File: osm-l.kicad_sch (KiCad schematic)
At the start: 48 parts, among them SW1 SW_KMR211NGLFS_SMD, SW2 SW_KMR211NGLFS_SMD, SW3 SW_KMR211NGLFS_SMD, U1 OSM-L_Carrier-side, U2 74AUP2G132, U3 74AUP2G132

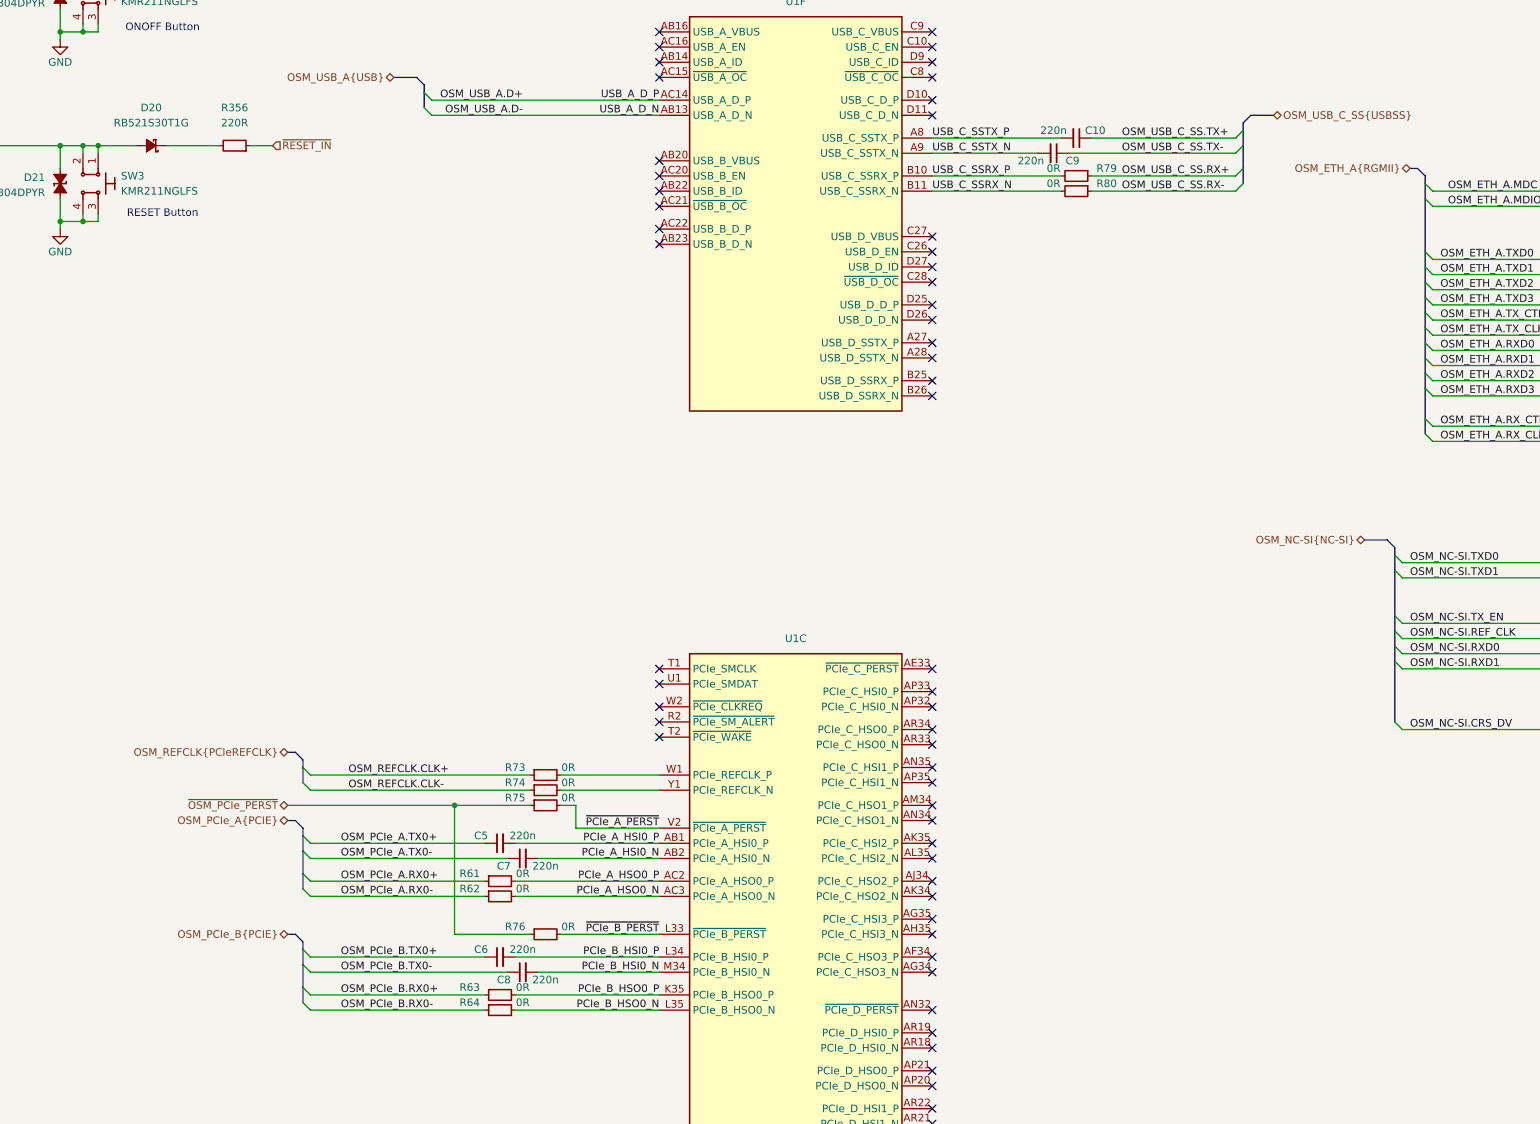
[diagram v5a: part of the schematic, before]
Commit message: [#83767] Remove PCIe/USB SS passives
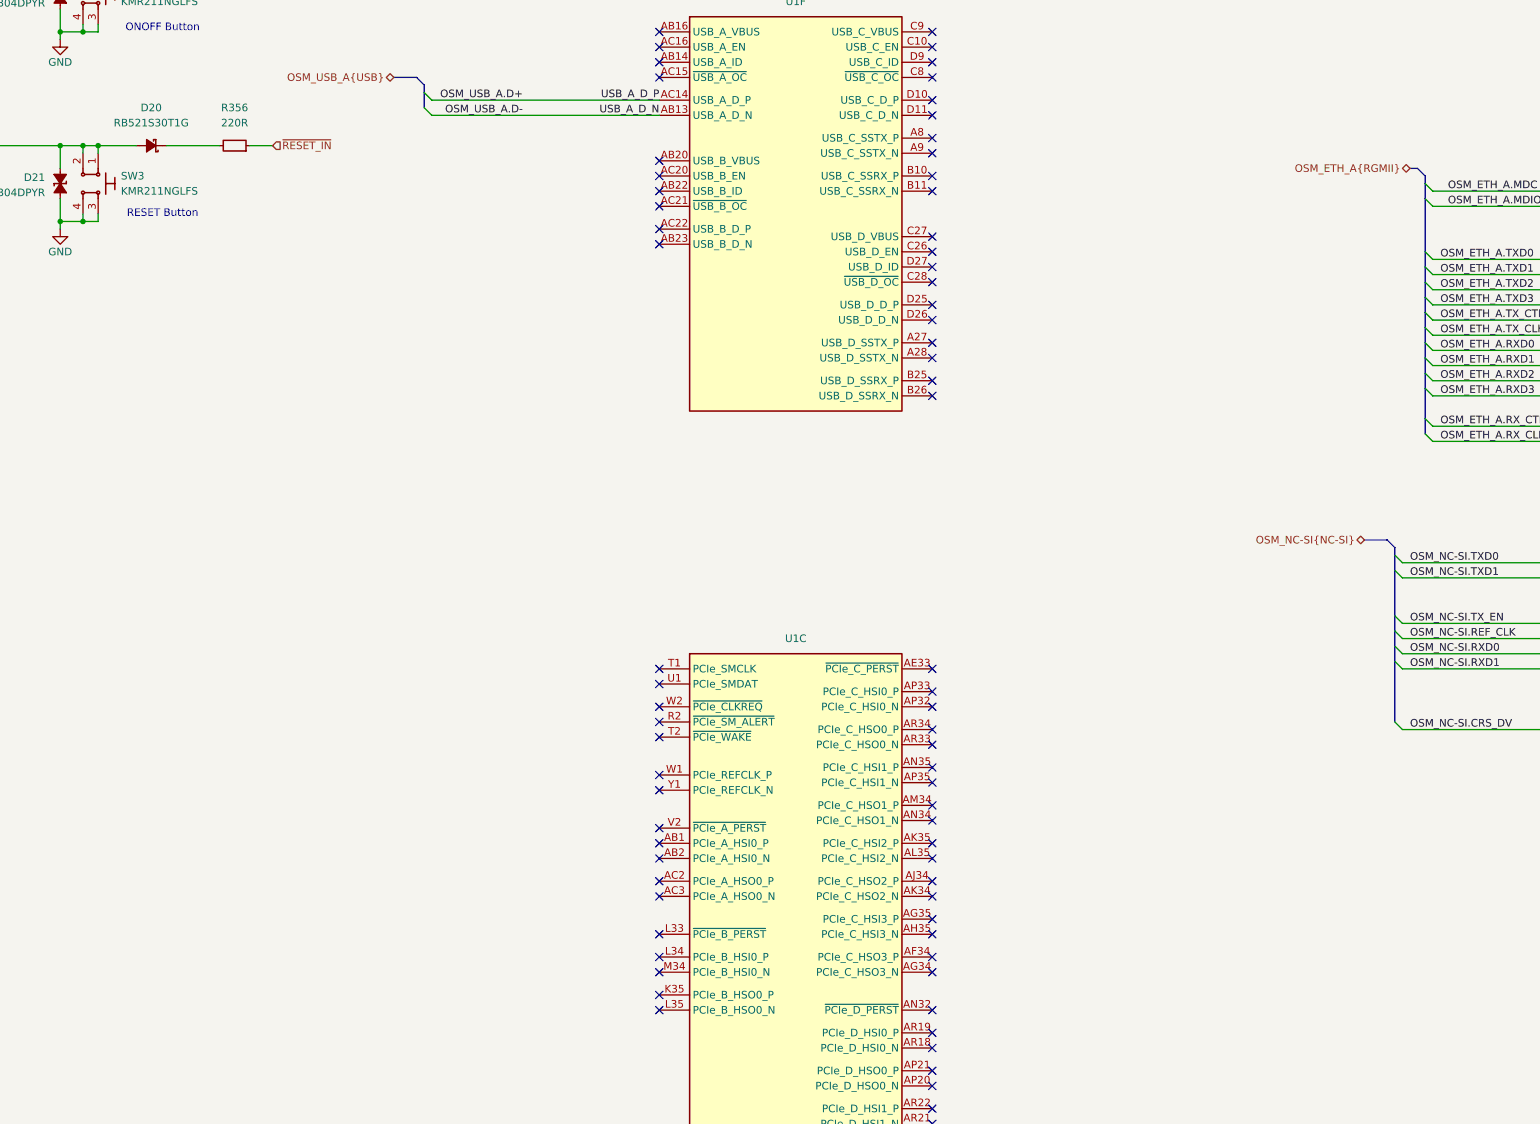
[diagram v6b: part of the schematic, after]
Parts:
- removed C10, C5, C6, C7, C8, C9: C_220n_0402, antmicro-footprints:C_0402_1005Metric, symbol antmicroCapacitors0402:C_220n_0402
- removed R61, R62, R63, R64, R73, R74, R75, R76, R79, R80: R_0R_0402, antmicro-footprints:R_0402_1005Metric, symbol antmicroResistors0402:R_0R_0402
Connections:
- net PCIe_A_HSI0_N: no longer names the net of U1.AB2 (PCIe_A_HSI0_N)
- net PCIe_A_HSI0_P: no longer names the net of U1.AB1 (PCIe_A_HSI0_P)
- net PCIe_A_HSO0_N: no longer names the net of U1.AC3 (PCIe_A_HSO0_N)
- net PCIe_A_HSO0_P: no longer names the net of U1.AC2 (PCIe_A_HSO0_P)
- net PCIe_B_HSI0_N: no longer names the net of U1.M34 (PCIe_B_HSI0_N)
- net PCIe_B_HSI0_P: no longer names the net of U1.L34 (PCIe_B_HSI0_P)
- net PCIe_B_HSO0_N: no longer names the net of U1.L35 (PCIe_B_HSO0_N)
- net PCIe_B_HSO0_P: no longer names the net of U1.K35 (PCIe_B_HSO0_P)
- net USB_C_SSRX_N: no longer names the net of U1.B11 (USB_C_SSRX_N)
- net USB_C_SSRX_P: no longer names the net of U1.B10 (USB_C_SSRX_P)
- net USB_C_SSTX_N: no longer names the net of U1.A9 (USB_C_SSTX_N)
- net USB_C_SSTX_P: no longer names the net of U1.A8 (USB_C_SSTX_P)
- net ~{PCIe_A_PERST}: no longer names the net of U1.V2 (~{PCIe_A_PERST})
- net ~{PCIe_B_PERST}: no longer names the net of U1.L33 (~{PCIe_B_PERST})
- no-connect marks 332 -> 348

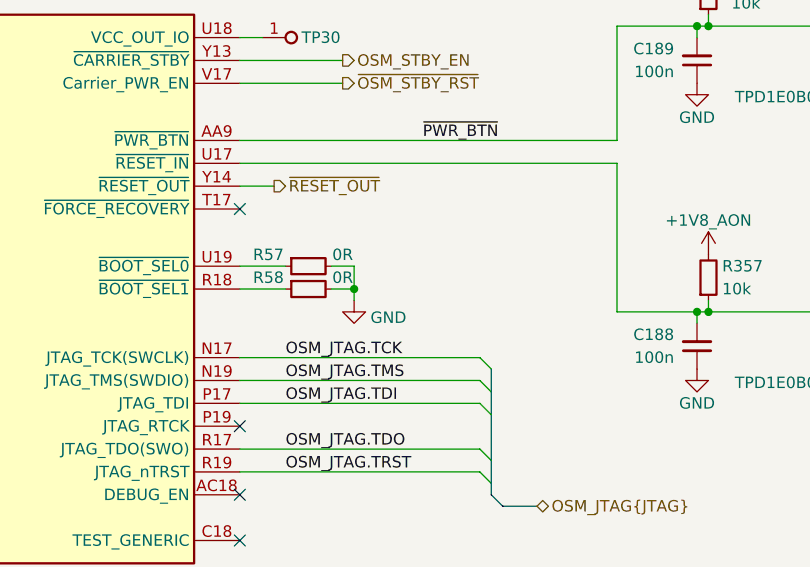
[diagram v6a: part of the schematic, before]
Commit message: [#83767] Add 12V DC input connector and BOOT_SEL switch
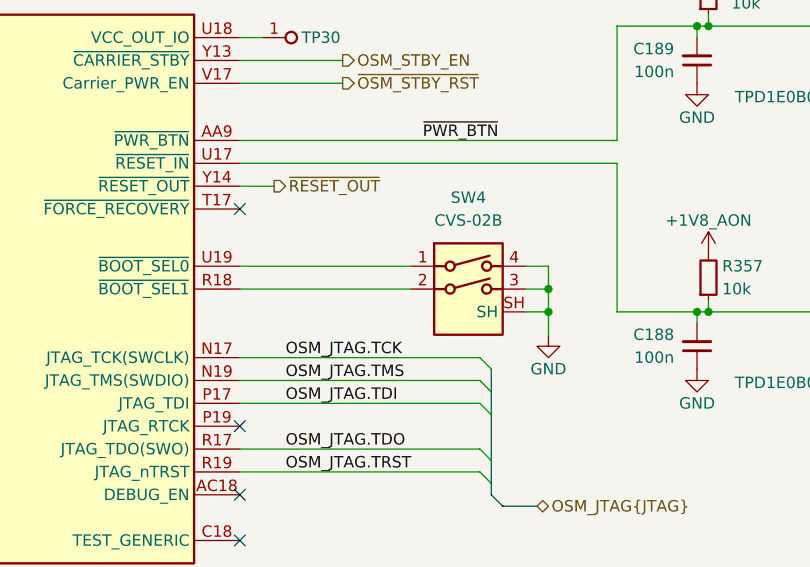
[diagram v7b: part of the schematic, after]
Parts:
- removed R57, R58: R_0R_0402, antmicro-footprints:R_0402_1005Metric, symbol antmicroResistors0402:R_0R_0402
- added SW4: SW_CVS-02B, antmicro-footprints:SW_DIP_SPSTx02_Slide_Copal_CVS-02xB_W5.9mm_P1mm, symbol antmicroSlideSwitches:SW_CVS-02B
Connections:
- net GND: now also SW4.3, SW4.4, SW4.SH
- net at U1.R18 (~{BOOT_SEL1}): now also SW4.2
- net at U1.U19 (~{BOOT_SEL0}): now also SW4.1

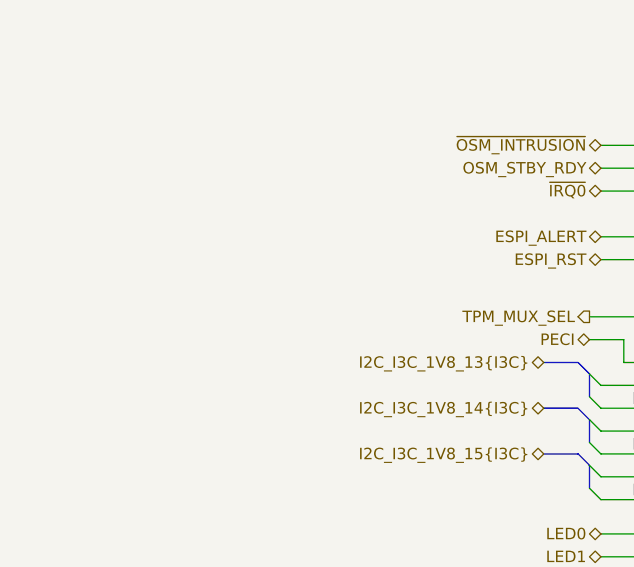
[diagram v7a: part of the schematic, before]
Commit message: [#83767] Add buttons to I2C_14
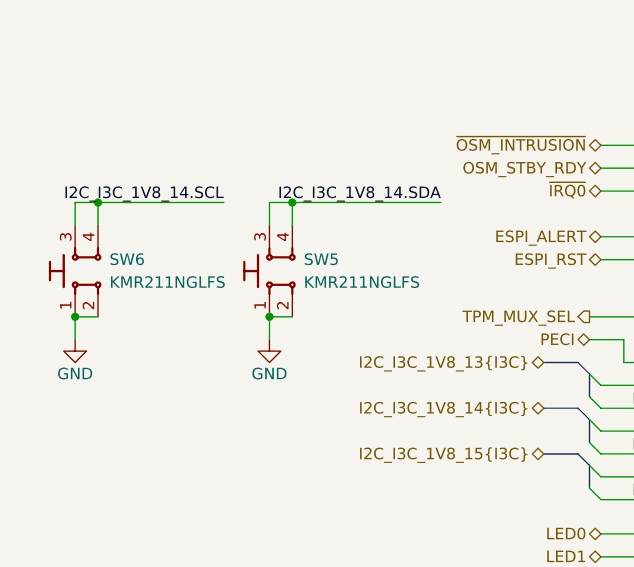
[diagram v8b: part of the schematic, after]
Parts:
- added SW5, SW6: SW_KMR211NGLFS_SMD, antmicro-footprints:SW_KMR211NGLFS_SMD, symbol antmicroPushbuttonSwitches:SW_KMR211NGLFS_SMD
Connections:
- net GND: now also SW5.1, SW5.2, SW6.1, SW6.2
- net I2C_I3C_1V8_14.SCL: now also SW6.3, SW6.4
- net I2C_I3C_1V8_14.SDA: now also SW5.3, SW5.4
